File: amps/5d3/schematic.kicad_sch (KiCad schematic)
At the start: 43 parts, among them T2 PP : 8

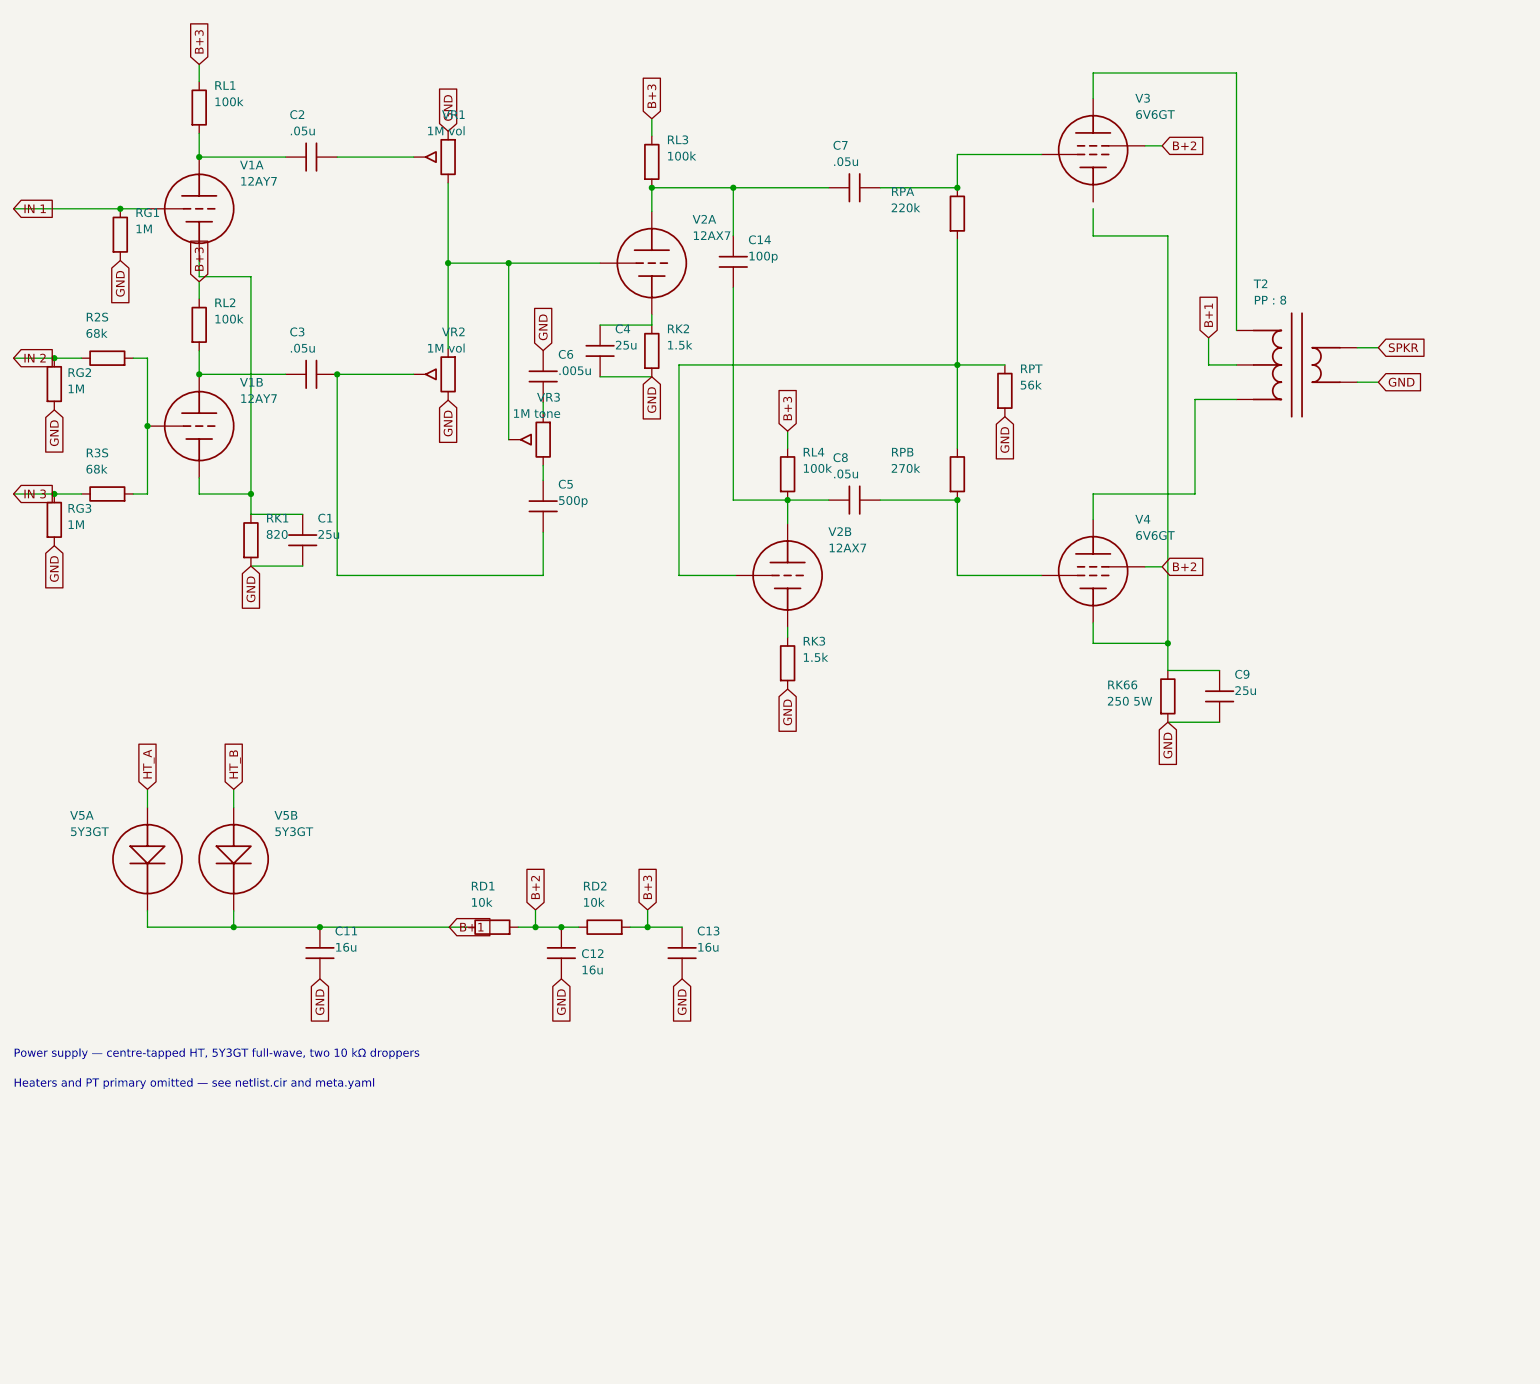
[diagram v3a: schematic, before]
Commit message: Fix: deterministic schematic ids and wires split at every join
- _u() is uuid5 over (amp id, emission order), so a regeneration of an
  unchanged script is byte-identical and a drift gate becomes possible
- write() splits wire segments at symbol pins, wire ends and junction dots,
  so the file connects exactly what the drawing shows under KiCad's
  endpoint-only semantics (270 pins were on a wire's interior; net
  partitions unchanged on all 38 sheets)
- all sheets regenerated; aa864-bassman title block was stale (draft) and
  now matches meta.yaml (verified)

Co-Authored-By: Claude Fable 5.1 <noreply@anthropic.com>
Claude-Session: https://claude.ai/code/session_01KBMfdh37HmCL2iWcBiL5J1
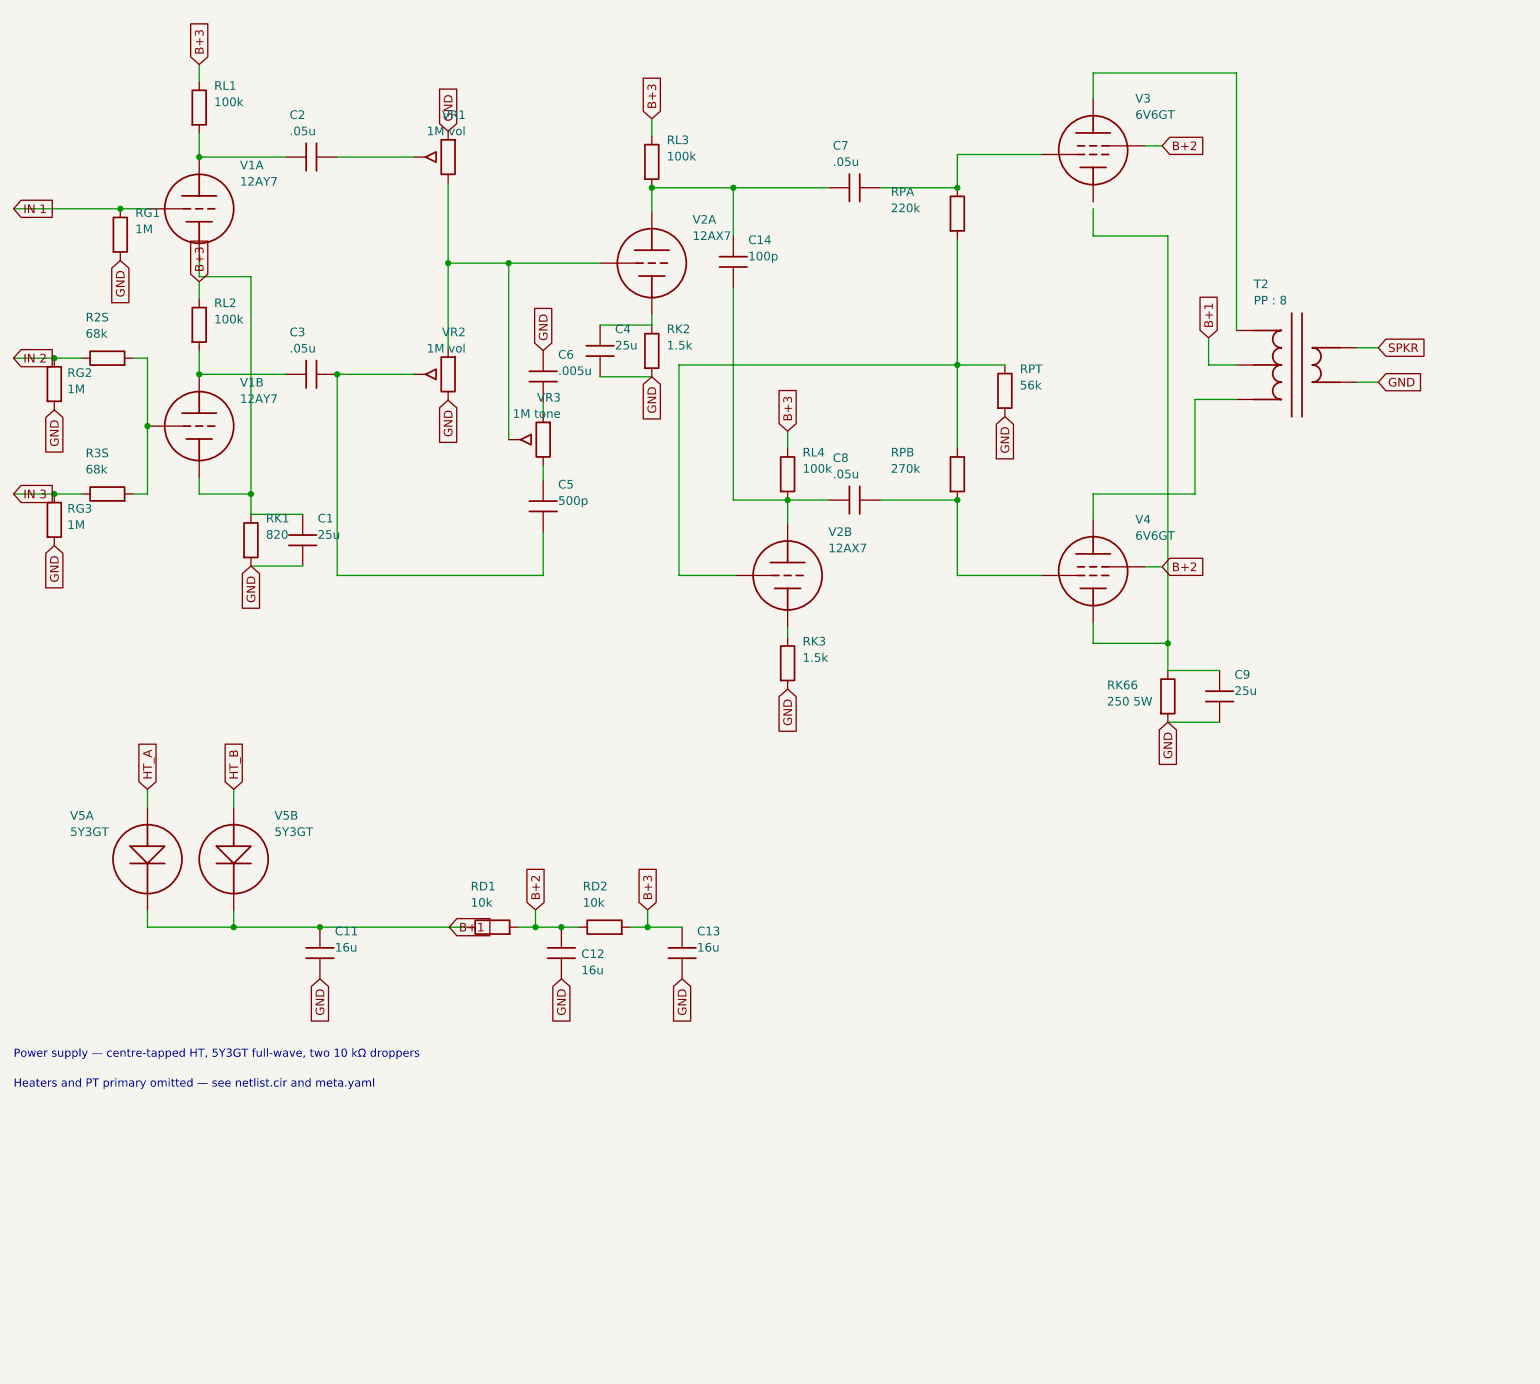
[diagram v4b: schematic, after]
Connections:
- net at C7.2, RPA.1: now also V3.2 (G1)
- net at V4.2 (G1): now also C8.2, RPB.2
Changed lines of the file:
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@@
   (wire (pts (xy 30.32 80.278) (xy 32.42 80.278))
     (stroke (width 0) (type default)))
-  (wire (pts (xy 32.42 60.278) (xy 32.42 80.278))
+  (wire (pts (xy 32.42 60.278) (xy 32.42 70.278))
+    (stroke (width 0) (type default)))
+  (wire (pts (xy 32.42 70.278) (xy 32.42 80.278))
     (stroke (width 0) (type default)))
   (junction (at 32.42 70.278) (diameter 0) (color 0 0 0 0))
@@
   (wire (pts (xy 40.04 80.278) (xy 47.66 80.278))
     (stroke (width 0) (type default)))
-  (wire (pts (xy 47.66 48.278) (xy 47.66 83.278))
+  (wire (pts (xy 47.66 48.278) (xy 47.66 80.278))
+    (stroke (width 0) (type default)))
+  (wire (pts (xy 47.66 80.278) (xy 47.66 83.278))
     (stroke (width 0) (type default)))
   (junction (at 47.66 80.278) (diameter 0) (color 0 0 0 0))
@@
     (property "Reference" "V2A" (at 112.7 39.878 0) (effects (font (size 1.27 1.27)) (justify left)))
     (property "Value" "12AX7" (at 112.7 42.278 0) (effects (font (size 1.27 1.27)) (justify left))))
-  (wire (pts (xy 76.7 46.278) (xy 99.08 46.278))
+  (wire (pts (xy 76.7 46.278) (xy 85.62 46.278))
+    (stroke (width 0) (type default)))
+  (wire (pts (xy 85.62 46.278) (xy 99.08 46.278))
     (stroke (width 0) (type default)))
   (wire (pts (xy 106.7 38.658) (xy 106.7 35.178))
@@
     (effects (font (size 1.27 1.27)) (justify right)))
   (junction (at 106.7 35.178) (diameter 0) (color 0 0 0 0))
-  (wire (pts (xy 106.7 35.178) (xy 132.75 35.178))
+  (wire (pts (xy 106.7 35.178) (xy 118.7 35.178))
+    (stroke (width 0) (type default)))
+  (wire (pts (xy 118.7 35.178) (xy 132.75 35.178))
     (stroke (width 0) (type default)))
   (junction (at 118.7 35.178) (diameter 0) (color 0 0 0 0))
@@
   (wire (pts (xy 118.7 49.898) (xy 118.7 81.178))
     (stroke (width 0) (type default)))
-  (wire (pts (xy 118.7 81.178) (xy 132.75 81.178))
+  (wire (pts (xy 118.7 81.178) (xy 126.7 81.178))
+    (stroke (width 0) (type default)))
+  (wire (pts (xy 126.7 81.178) (xy 132.75 81.178))
     (stroke (width 0) (type default)))
   (junction (at 126.7 81.178) (diameter 0) (color 0 0 0 0))
@@
   (wire (pts (xy 151.7 35.178) (xy 151.7 30.278))
     (stroke (width 0) (type default)))
-  (wire (pts (xy 151.7 30.278) (xy 164.1 30.278))
+  (wire (pts (xy 151.7 30.278) (xy 164.08 30.278))
+    (stroke (width 0) (type default)))
+  (wire (pts (xy 164.08 30.278) (xy 164.1 30.278))
     (stroke (width 0) (type default)))
   (symbol (lib_id "cx:C") (at 136.56 81.178 90) (unit 1)
@@
   (wire (pts (xy 151.7 81.178) (xy 151.7 92.278))
     (stroke (width 0) (type default)))
-  (wire (pts (xy 151.7 92.278) (xy 164.1 92.278))
+  (wire (pts (xy 151.7 92.278) (xy 164.08 92.278))
+    (stroke (width 0) (type default)))
+  (wire (pts (xy 164.08 92.278) (xy 164.1 92.278))
     (stroke (width 0) (type default)))
   (symbol (lib_id "cx:R") (at 151.7 38.988 0) (unit 1)
@@
   (wire (pts (xy 171.7 102.278) (xy 182.7 102.278))
     (stroke (width 0) (type default)))
-  (wire (pts (xy 182.7 42.278) (xy 182.7 106.278))
+  (wire (pts (xy 182.7 42.278) (xy 182.7 102.278))
+    (stroke (width 0) (type default)))
+  (wire (pts (xy 182.7 102.278) (xy 182.7 106.278))
     (stroke (width 0) (type default)))
   (junction (at 182.7 102.278) (diameter 0) (color 0 0 0 0))
@@
   (wire (pts (xy 45.12 141.678) (xy 45.12 144.078))
     (stroke (width 0) (type default)))
-  (wire (pts (xy 32.42 144.078) (xy 76.87 144.078))
+  (wire (pts (xy 32.42 144.078) (xy 45.12 144.078))
+    (stroke (width 0) (type default)))
+  (wire (pts (xy 45.12 144.078) (xy 57.82 144.078))
+    (stroke (width 0) (type default)))
+  (wire (pts (xy 57.82 144.078) (xy 76.87 144.078))
     (stroke (width 0) (type default)))
   (junction (at 45.12 144.078) (diameter 0) (color 0 0 0 0))
@@
     (property "Reference" "RD1" (at 80.02 138.078 270) (effects (font (size 1.27 1.27)) (justify left)))
     (property "Value" "10k" (at 80.02 140.478 270) (effects (font (size 1.27 1.27)) (justify left))))
-  (wire (pts (xy 87.03 144.078) (xy 95.92 144.078))
+  (wire (pts (xy 87.03 144.078) (xy 89.57 144.078))
+    (stroke (width 0) (type default)))
+  (wire (pts (xy 89.57 144.078) (xy 93.38 144.078))
+    (stroke (width 0) (type default)))
+  (wire (pts (xy 93.38 144.078) (xy 95.92 144.078))
     (stroke (width 0) (type default)))
   (junction (at 89.57 144.078) (diameter 0) (color 0 0 0 0))
@@
     (property "Reference" "RD2" (at 96.53 138.078 270) (effects (font (size 1.27 1.27)) (justify left)))
     (property "Value" "10k" (at 96.53 140.478 270) (effects (font (size 1.27 1.27)) (justify left))))
-  (wire (pts (xy 103.54 144.078) (xy 111.16 144.078))
+  (wire (pts (xy 103.54 144.078) (xy 106.08 144.078))
+    (stroke (width 0) (type default)))
+  (wire (pts (xy 106.08 144.078) (xy 111.16 144.078))
     (stroke (width 0) (type default)))
   (junction (at 106.08 144.078) (diameter 0) (color 0 0 0 0))

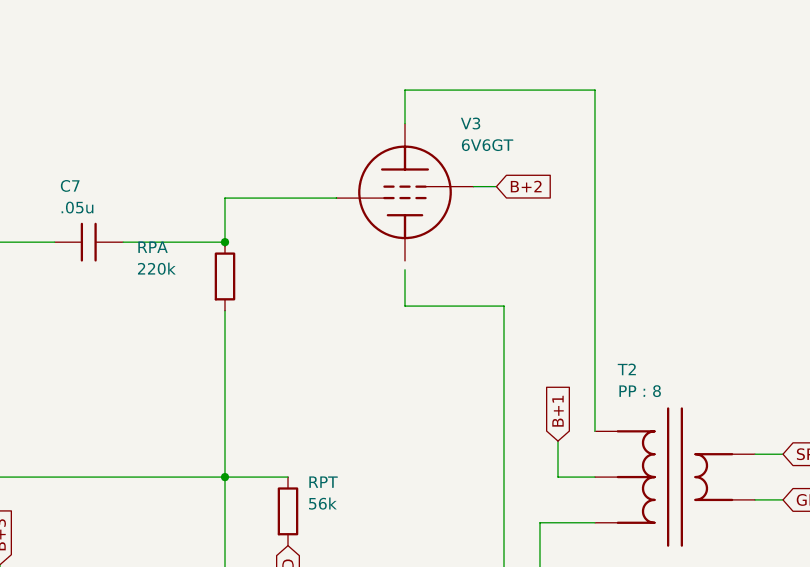
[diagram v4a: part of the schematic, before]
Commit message: Fix: schematic wiring on the tweed family, jtm45 and 6161
- pot cold lugs: s.gnd() sat 3.81 mm below cx:POT pin 3 on nine sheets
  (19 pins); every flag now lands on the lug
- retyped coordinates replaced by helper returns (5e5a OT pins alone freed
  nine pins; 5d3 V3 cathode, 5f10 RKB, 5e6a CBS, 5f2a dropper, grid leaks)
- shorts only verify_schematic_nets could see: 5e3 cathode bus through V4's
  screen pin (B+2 tied to the cathodes), C7 through RG6A, PI leak through
  RGPI, C8 on the cathode not the tail; 5f10 the same RGPI/C7 pair; 5e5a
  presence feed down the tube column; 5e6a RFB loop through RL3
- three dated waivers: two-terminal rheostat far lugs (5e6a VR5, 6161 VR3/VR4)

Co-Authored-By: Claude Fable 5.1 <noreply@anthropic.com>
Claude-Session: https://claude.ai/code/session_01KBMfdh37HmCL2iWcBiL5J1
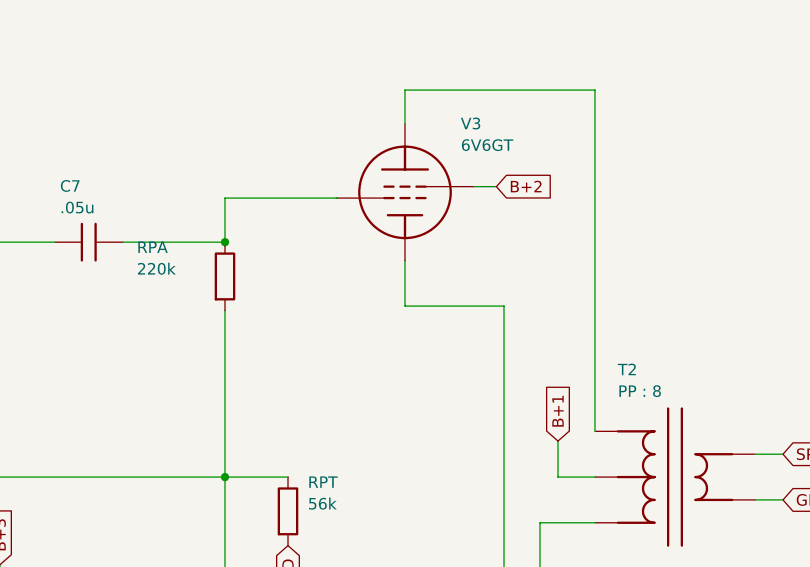
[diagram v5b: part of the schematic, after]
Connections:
- net at C9.1, RK66.1, V4.4 (K): now also V3.4 (K)
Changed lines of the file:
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@@
   (global_label "B+2" (shape input) (at 181.86 91.008 0)
     (effects (font (size 1.27 1.27)) (justify left)))
-  (wire (pts (xy 171.7 38.263) (xy 171.7 42.278))
+  (wire (pts (xy 171.7 37.263) (xy 171.7 42.278))
     (stroke (width 0) (type default)))
   (wire (pts (xy 171.7 42.278) (xy 182.7 42.278))
